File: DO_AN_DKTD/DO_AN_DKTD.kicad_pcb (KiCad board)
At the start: 2 copper layers, 90.2 x 65.7 mm, 60 parts, among them J1 Conn_01x03, J2 Conn_01x02, J3 Conn_01x07, J4 Conn_01x04, J5 Conn_01x02, Q1 NPN, Q2 NPN, Q3 NPN, Q4 NPN, SW2 RotaryEncoder_Switch, U1 AMS1117, U2 74HC595, U3 MOC3020M, U4 PC817, U5 DevKitSTM32

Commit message: code update
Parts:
- added R30: 4k7, IVS_FOOTPRINTS:R0603, B.Cu at (161.3, 125.4)
- added R31: 4k7, IVS_FOOTPRINTS:R0603, B.Cu at (161.3, 122.3)
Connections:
- U5 pad 11: /SER -> unconnected-(U5-PA6-Pad11)
- U5 pad 12: /OE -> unconnected-(U5-PA7-Pad12)
- U5 pad 26: unconnected-(U5-PB7-Pad26) -> /OE
- U5 pad 27: unconnected-(U5-PB6-Pad27) -> /SER
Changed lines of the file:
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@@
   (net 62 "unconnected-(U5-3v3-Pad18)")
   (net 63 "unconnected-(U5-3v3-Pad21)")
-  (net 64 "unconnected-(U5-PB6-Pad27)")
+  (net 64 "unconnected-(U5-PA6-Pad11)")
   (net 65 "unconnected-(U5-PB5-Pad28)")
   (net 66 "unconnected-(U5-PA12-Pad32)")
@@
   (net 81 "unconnected-(U5-PA4-Pad9)")
   (net 82 "unconnected-(U5-PA5-Pad10)")
-  (net 83 "unconnected-(U5-PB7-Pad26)")
+  (net 83 "unconnected-(U5-PA7-Pad12)")
   (net 84 "Net-(R15-Pad1)")
   (net 85 "/5vin")
@@
       (net 82 "unconnected-(U5-PA5-Pad10)") (pinfunction "PA5") (pintype "input+no_connect"))
     (pad "11" thru_hole circle (at -7.62 2.54 270) (size 1.524 1.524) (drill 0.762) (layers "*.Cu" "*.Mask")
-      (net 45 "/SER") (pinfunction "PA6") (pintype "input"))
+      (net 64 "unconnected-(U5-PA6-Pad11)") (pinfunction "PA6") (pintype "input+no_connect"))
     (pad "12" thru_hole circle (at -7.62 5.08 270) (size 1.524 1.524) (drill 0.762) (layers "*.Cu" "*.Mask")
-      (net 48 "/OE") (pinfunction "PA7") (pintype "input"))
+      (net 83 "unconnected-(U5-PA7-Pad12)") (pinfunction "PA7") (pintype "input+no_connect"))
     (pad "13" thru_hole circle (at -7.62 7.62 270) (size 1.524 1.524) (drill 0.762) (layers "*.Cu" "*.Mask")
       (net 53 "/AC_DET") (pinfunction "PB0") (pintype "input"))
@@
       (net 47 "/RCLK") (pinfunction "PB8") (pintype "input"))
     (pad "26" thru_hole circle (at 7.62 -10.16 270) (size 1.524 1.524) (drill 0.762) (layers "*.Cu" "*.Mask")
-      (net 83 "unconnected-(U5-PB7-Pad26)") (pinfunction "PB7") (pintype "input+no_connect"))
+      (net 48 "/OE") (pinfunction "PB7") (pintype "input"))
     (pad "27" thru_hole circle (at 7.62 -7.62 270) (size 1.524 1.524) (drill 0.762) (layers "*.Cu" "*.Mask")
-      (net 64 "unconnected-(U5-PB6-Pad27)") (pinfunction "PB6") (pintype "input+no_connect"))
+      (net 45 "/SER") (pinfunction "PB6") (pintype "input"))
     (pad "28" thru_hole circle (at 7.62 -5.08 270) (size 1.524 1.524) (drill 0.762) (layers "*.Cu" "*.Mask")
       (net 65 "unconnected-(U5-PB5-Pad28)") (pinfunction "PB5") (pintype "input+no_connect"))
@@
   )
   (footprint "IVS_FOOTPRINTS:R0603" (layer "B.Cu")
+    (at 161.255 125.4)
+    (descr "Resistor SMD 0603 (1608 Metric), square (rectangular) end terminal, IPC_7351 nominal, (Body size source: IPC-SM-782 page 72, https://www.pcb-3d.com/wordpress/wp-content/uploads/ipc-sm-782a_amendment_1_and_2.pdf), generated with kicad-footprint-generator")
+    (tags "resistor")
+    (property "Sheetfile" "DO_AN_DKTD.kicad_sch")
+    (property "Sheetname" "")
+    (property "ki_description" "Resistor")
+    (property "ki_keywords" "R res resistor")
+    (attr smd)
+    (fp_text reference "R30" (at -0.025 -1.5) (layer "B.SilkS")
+        (effects (font (size 0.6 0.6) (thickness 0.15)) (justify mirror))
+    )
+    (fp_text value "4k7" (at 0 -1.43) (layer "B.Fab") hide
+        (effects (font (size 1 1) (thickness 0.15)) (justify mirror))
+    )
+    (fp_text user "${REFERENCE}" (at 0 0) (layer "B.Fab") hide
+        (effects (font (size 0.4 0.4) (thickness 0.06)) (justify mirror))
+    )
+    (fp_rect (start -1.63 0.85) (end 1.63 -0.9)
+      (stroke (width 0.25) (type solid)) (fill none) (layer "B.SilkS"))
+    (fp_rect (start -1.78 1) (end 1.795 -1.05)
+      (stroke (width 0.05) (type solid)) (fill none) (layer "B.CrtYd"))
+    (fp_line (start -0.805 -0.4125) (end -0.805 0.4125)
+      (stroke (width 0.1) (type solid)) (layer "B.Fab"))
+    (fp_line (start -0.805 0.4125) (end 0.795 0.4125)
+      (stroke (width 0.1) (type solid)) (layer "B.Fab"))
+    (fp_line (start 0.795 -0.4125) (end -0.805 -0.4125)
+      (stroke (width 0.1) (type solid)) (layer "B.Fab"))
+    (fp_line (start 0.795 0.4125) (end 0.795 -0.4125)
+      (stroke (width 0.1) (type solid)) (layer "B.Fab"))
+    (pad "1" smd roundrect (at -0.83 0) (size 1 1) (layers "B.Cu" "B.Paste" "B.Mask") (roundrect_rratio 0.25)
+      (net 3 "+3V3") (pintype "passive"))
+    (pad "2" smd roundrect (at 0.82 0) (size 1 1) (layers "B.Cu" "B.Paste" "B.Mask") (roundrect_rratio 0.25)
+      (net 21 "/SCL") (pintype "passive"))
+    (model "${IOTVISION_3D}/RESISTOR/Resistor 0603.step"
+      (offset (xyz -0.75 1.15 0))
+      (scale (xyz 1 1 1))
+      (rotate (xyz -90 0 0))
+    )
+  )
+  (footprint "IVS_FOOTPRINTS:R0603" (layer "B.Cu")
     (at 144.7825 106.625 180)
     (descr "Resistor SMD 0603 (1608 Metric), square (rectangular) end terminal, IPC_7351 nominal, (Body size source: IPC-SM-782 page 72, https://www.pcb-3d.com/wordpress/wp-content/uploads/ipc-sm-782a_amendment_1_and_2.pdf), generated with kicad-footprint-generator")
@@
       (scale (xyz 1 1 1))
       (rotate (xyz -90 0 0))
+    )
+  )
+  (footprint "IVS_FOOTPRINTS:R0603" (layer "B.Cu")
+    (at 161.255 122.3)
+    (descr "Resistor SMD 0603 (1608 Metric), square (rectangular) end terminal, IPC_7351 nominal, (Body size source: IPC-SM-782 page 72, https://www.pcb-3d.com/wordpress/wp-content/uploads/ipc-sm-782a_amendment_1_and_2.pdf), generated with kicad-footprint-generator")
+    (tags "resistor")
+    (property "Sheetfile" "DO_AN_DKTD.kicad_sch")
+    (property "Sheetname" "")
+    (property "ki_description" "Resistor")
+    (property "ki_keywords" "R res resistor")
+    (attr smd)
+    (fp_text reference "R31" (at -0.025 -1.5) (layer "B.SilkS")
+        (effects (font (size 0.6 0.6) (thickness 0.15)) (justify mirror))
+    )
+    (fp_text value "4k7" (at 0 -1.43) (layer "B.Fab") hide
+        (effects (font (size 1 1) (thickness 0.15)) (justify mirror))
+    )
+    (fp_text user "${REFERENCE}" (at 0 0) (layer "B.Fab") hide
+        (effects (font (size 0.4 0.4) (thickness 0.06)) (justify mirror))
+    )
+    (fp_rect (start -1.63 0.85) (end 1.63 -0.9)
+      (stroke (width 0.25) (type solid)) (fill none) (layer "B.SilkS"))
+    (fp_rect (start -1.78 1) (end 1.795 -1.05)
+      (stroke (width 0.05) (type solid)) (fill none) (layer "B.CrtYd"))
+    (fp_line (start -0.805 -0.4125) (end -0.805 0.4125)
+      (stroke (width 0.1) (type solid)) (layer "B.Fab"))
+    (fp_line (start -0.805 0.4125) (end 0.795 0.4125)
+      (stroke (width 0.1) (type solid)) (layer "B.Fab"))
+    (fp_line (start 0.795 -0.4125) (end -0.805 -0.4125)
+      (stroke (width 0.1) (type solid)) (layer "B.Fab"))
+    (fp_line (start 0.795 0.4125) (end 0.795 -0.4125)
+      (stroke (width 0.1) (type solid)) (layer "B.Fab"))
+    (pad "1" smd roundrect (at -0.83 0) (size 1 1) (layers "B.Cu" "B.Paste" "B.Mask") (roundrect_rratio 0.25)
+      (net 3 "+3V3") (pintype "passive"))
+    (pad "2" smd roundrect (at 0.82 0) (size 1 1) (layers "B.Cu" "B.Paste" "B.Mask") (roundrect_rratio 0.25)
+      (net 22 "/SDA") (pintype "passive"))
+    (model "${IOTVISION_3D}/RESISTOR/Resistor 0603.step"
+      (offset (xyz -0.75 1.15 0))
+      (scale (xyz 1 1 1))
+      (rotate (xyz -90 0 0))

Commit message: completed layout PCB Ver 1.0
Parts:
- added BT1: CR1220, IVS_FOOTPRINTS:BatteryHolder_CR1220, F.Cu at (137.0, 80.0)
- added BZ1: Buzzer, Buzzer_Beeper:Buzzer_12x9.5RM7.6, F.Cu at (137.5, 96.6)
- added C10: 100nF, IVS_FOOTPRINTS:C_0603, F.Cu at (130.5, 126.5)
- added C11: 100nF, IVS_FOOTPRINTS:C_0603, F.Cu at (145.9, 113.0)
- added C12: 22pF, IVS_FOOTPRINTS:C_0603, F.Cu at (126.5, 115.0)
- added C13: 22pF, IVS_FOOTPRINTS:C_0603, F.Cu at (126.5, 112.0)
- added C14: 10uF, IVS_FOOTPRINTS:C_0603, F.Cu at (119.1, 89.0)
- added C15: 1uF, IVS_FOOTPRINTS:C_0603, F.Cu at (164.2, 129.3)
- added C16: 1uF, IVS_FOOTPRINTS:C_0603, F.Cu at (144.7, 125.7)
- added C17: 1uF, IVS_FOOTPRINTS:C_0603, F.Cu at (148.0, 125.7)
- added C18: 1uF, IVS_FOOTPRINTS:C_0603, F.Cu at (151.4, 125.7)
- added C19: 100nF, IVS_FOOTPRINTS:C_0603, F.Cu at (119.1, 90.7)
- added C20: 10uF, IVS_FOOTPRINTS:C_0603, F.Cu at (119.1, 92.5)
- added C21: 100nF, IVS_FOOTPRINTS:C_0603, F.Cu at (119.1, 94.0)
- added C22: 1uF, IVS_FOOTPRINTS:C_0603, F.Cu at (118.0, 138.5)
- added C23: 100nF, IVS_FOOTPRINTS:C_0603, F.Cu at (116.5, 138.5)
- added C24: 10uF, IVS_FOOTPRINTS:C_0805, F.Cu at (127.5, 65.8)
- added C25: 1uF, IVS_FOOTPRINTS:C_0603, F.Cu at (125.4, 65.8)
- added C26: 100nF, IVS_FOOTPRINTS:C_0603, F.Cu at (128.2, 69.2)
- added C27: 10uF, IVS_FOOTPRINTS:C_0805, F.Cu at (112.5, 53.7)
- added C29: 1uF, IVS_FOOTPRINTS:C_0603, F.Cu at (164.2, 133.0)
- added C30: 1uF, IVS_FOOTPRINTS:C_0603, F.Cu at (164.2, 139.2)
- added C31: 1uF, IVS_FOOTPRINTS:C_0603, F.Cu at (168.4, 122.8)
- added C32: 100nF, IVS_FOOTPRINTS:C_0603, F.Cu at (168.4, 124.2)
- added C33: 100nF, IVS_FOOTPRINTS:C_0603, F.Cu at (111.0, 115.8)
- added C34: 100nF, IVS_FOOTPRINTS:C_0603, F.Cu at (120.0, 118.8)
- added C35: 100nF, IVS_FOOTPRINTS:C_0603, F.Cu at (112.2, 107.8)
- added C36: 100nF, IVS_FOOTPRINTS:C_0603, F.Cu at (123.3, 110.6)
- added D+: TestPoint, TestPoint:TestPoint_THTPad_D2.0mm_Drill1.0mm, F.Cu at (100.4, 103.8)
- added D-: TestPoint, TestPoint:TestPoint_THTPad_D2.0mm_Drill1.0mm, F.Cu at (102.9, 103.8)
- added D4: BAT54C, IVS_FOOTPRINTS:SOT23-3, F.Cu at (120.8, 74.2)
- added D5: SMF05C, IVS_FOOTPRINTS:TSSOP-6, F.Cu at (122.1, 135.1)
- added D6: SS54, IVS_FOOTPRINTS:D_SMA, F.Cu at (120.0, 61.3)
- added D7: D_Schottky, IVS_FOOTPRINTS:D_SOD323, F.Cu at (125.2, 69.3)
- added D8: SS54, IVS_FOOTPRINTS:D_SMA, F.Cu at (132.6, 64.2)
- added F3: Fuse, IVS_FOOTPRINTS:Fuse_1812_4532Metric, F.Cu at (141.8, 59.2)
- added G***: LOGO, IVS_FOOTPRINTS:LoGo_ST_2.5x1.5mm, F.Cu at (158.1, 129.8)
- added G***: LOGO, IVS_FOOTPRINTS:LoGo_IDF_2.5x2.5mm, F.Cu at (158.1, 138.3)
- added G***: LOGO, IVS_FOOTPRINTS:LoGo_1412_10x8mm, F.Cu at (110.6, 121.7)
- added G***: LOGO, IVS_FOOTPRINTS:LoGo_ST_2.5x1.5mm, F.Cu at (117.0, 112.8)
- added G***: LOGO, IVS_FOOTPRINTS:LoGo_IDF_2.5x2.5mm, F.Cu at (179.3, 134.3)
- added G***: LOGO, IVS_FOOTPRINTS:LoGo_1412_10x8mm, B.Cu at (164.6, 68.3)
- added IC1: RTC_DS3231M, IVS_FOOTPRINTS:SOIC-16W_7.5x10.3mm_P1.27mm, F.Cu at (121.5, 82.0)
- added J10: Jack-DC, IVS_FOOTPRINTS:BarrelJack_Wuerth_6941xx301002, F.Cu at (134.2, 55.2)
- added J6: , Connector_PinHeader_2.54mm:PinHeader_1x06_P2.54mm_Vertical, F.Cu at (180.8, 120.0)
- added J7: Conn_01x05_Male, Connector_PinHeader_2.54mm:PinHeader_1x05_P2.54mm_Vertical, F.Cu at (109.8, 88.0)
- added J8: Micro_SD_Card_Det1, IVS_FOOTPRINTS:MicroSD_Socket_9P, F.Cu at (132.4, 139.8)
- added J9: USB_C_Receptacle, IVS_FOOTPRINTS:USB_C_Receptacle_XKB_U262-16XN-4BVC11, F.Cu at (101.0, 110.8)
- added L1: 68uH 2A, IVS_FOOTPRINTS:L_10.4x10.4_H4.8, F.Cu at (122.0, 53.5)
- added LE2: 5631AS, IVS_FOOTPRINTS:7Segment_4led_Cathode_30x14mm, F.Cu at (175.7, 108.5)
- added LE3: Led, IVS_FOOTPRINTS:LED_0603, F.Cu at (136.6, 115.8)
- added LE4: Led, IVS_FOOTPRINTS:LED_0603, F.Cu at (132.6, 115.8)
- added LE5: Led, IVS_FOOTPRINTS:LED_0603, F.Cu at (134.6, 115.8)
- added LE6: Led, IVS_FOOTPRINTS:LED_0603, F.Cu at (106.5, 93.5)
- added LE7: Led, IVS_FOOTPRINTS:LED_0603, F.Cu at (106.2, 48.8)
- added LE8: Led, IVS_FOOTPRINTS:LED_0603, F.Cu at (106.2, 50.2)
- added LE9: Led, IVS_FOOTPRINTS:LED_0603, F.Cu at (106.5, 100.0)
- added MI: TestPoint, TestPoint:TestPoint_THTPad_D2.0mm_Drill1.0mm, F.Cu at (120.3, 142.9)
- added MO: TestPoint, TestPoint:TestPoint_THTPad_D2.0mm_Drill1.0mm, F.Cu at (120.3, 137.8)
- added Q10: P_Mosfet, IVS_FOOTPRINTS:SOT23-3, F.Cu at (132.8, 67.5)
- added Q5: NPN, IVS_FOOTPRINTS:SOT23-3, F.Cu at (157.5, 110.1)
- added Q6: NPN, IVS_FOOTPRINTS:SOT23-3, F.Cu at (157.5, 106.7)
- added Q7: NPN, IVS_FOOTPRINTS:SOT23-3, F.Cu at (157.5, 103.3)
- added Q8: NPN, IVS_FOOTPRINTS:SOT23-3, F.Cu at (157.5, 113.7)
- added Q9: N_Mosfet, IVS_FOOTPRINTS:SOT23-3, F.Cu at (125.2, 97.5)
- added R32: 12k, IVS_FOOTPRINTS:R_0603, F.Cu at (126.7, 69.2)
- added R36: 2k, IVS_FOOTPRINTS:R_0603, F.Cu at (154.7, 110.1)
- added R37: 2k, IVS_FOOTPRINTS:R_0603, F.Cu at (154.7, 106.7)
- added R38: 2k, IVS_FOOTPRINTS:R_0603, F.Cu at (154.7, 103.3)
- added R39: 2k, IVS_FOOTPRINTS:R_0603, F.Cu at (154.7, 113.7)
- added R40: 1M, IVS_FOOTPRINTS:R_0603, F.Cu at (125.0, 113.8)
- added R41: 1k, IVS_FOOTPRINTS:R_0603, F.Cu at (123.5, 74.2)
- added R42: 100, IVS_FOOTPRINTS:R_0603, F.Cu at (164.0, 122.8)
- added R43: 10k, IVS_FOOTPRINTS:R_0603, F.Cu at (164.2, 136.0)
- added R44: 1k, IVS_FOOTPRINTS:R_0603, F.Cu at (136.6, 112.3)
- added R45: 10k, IVS_FOOTPRINTS:R_0603, F.Cu at (164.2, 142.2)
- added R46: 10k, IVS_FOOTPRINTS:R_0603, F.Cu at (164.2, 126.3)
- added R47: 1k, IVS_FOOTPRINTS:R_0603, F.Cu at (132.6, 112.2)
- added R48: 1k, IVS_FOOTPRINTS:R_0603, F.Cu at (134.6, 112.2)
- added R50: 1k, IVS_FOOTPRINTS:R_0603, F.Cu at (109.2, 48.8)
- added R51: 1k, IVS_FOOTPRINTS:R_0603, F.Cu at (109.2, 50.2)
- added R55: 4k7, IVS_FOOTPRINTS:R_0603, F.Cu at (111.0, 110.8)
- added R58: 100R, IVS_FOOTPRINTS:R_0603, F.Cu at (112.2, 106.3)
- added R59: 100R, IVS_FOOTPRINTS:R_0603, F.Cu at (122.6, 108.1)
- added R60: 1M, IVS_FOOTPRINTS:R_0603, F.Cu at (125.2, 100.4)
- added R61: 10K, IVS_FOOTPRINTS:R_0603, F.Cu at (115.8, 104.5)
- added R62: 10K, IVS_FOOTPRINTS:R_0603, F.Cu at (120.0, 120.2)
- added REF**: MountingHole_3.2mm_M3_Pad_Via, MountingHole:MountingHole_3.2mm_M3_Pad_Via, F.Cu at (186.5, 121.2)
- added REF**: MountingHole_3.2mm_M3_Pad_Via, MountingHole:MountingHole_3.2mm_M3_Pad_Via, F.Cu at (186.5, 72.8)
- added REF**: MountingHole_3.2mm_M3_Pad_Via, MountingHole:MountingHole_3.2mm_M3_Pad_Via, F.Cu at (101.5, 121.2)
- added REF**: MountingHole_3.2mm_M3_Pad_Via, MountingHole:MountingHole_3.2mm_M3_Pad_Via, F.Cu at (101.5, 72.8)
- added SCK: TestPoint, TestPoint:TestPoint_THTPad_D2.0mm_Drill1.0mm, F.Cu at (120.3, 140.3)
- added SW1: RotaryEncoder_Switch, IVS_FOOTPRINTS:RotaryEncoder_Alps_EC11E-Switch_Vertical_H20mm, F.Cu at (149.8, 135.7)
- added SW3: SW_Push, IVS_FOOTPRINTS:SW_SPST_PTS810, F.Cu at (161.5, 134.5)
- added SW4: SW_Push, IVS_FOOTPRINTS:SW_SPST_PTS810, F.Cu at (161.5, 127.8)
- added U10: ESP-07, IVS_FOOTPRINTS:ESP8266-07__ESP32-C3-12F, F.Cu at (184.2, 126.1)
- added U6: 74HC595, IVS_FOOTPRINTS:SOIC-16W_3.92x10.2mm, F.Cu at (147.9, 107.0)
- added U7: STM32F103C8Tx, IVS_FOOTPRINTS:LQFP-48_7x7mm_P0.5mm, F.Cu at (117.0, 112.8)
- added U8: 24C32N, IVS_FOOTPRINTS:SOIC-8_3.9x4.9mm_P1.27mm, F.Cu at (120.2, 98.5)
- added U9: Ai-Thinker-Ra-02, IVS_FOOTPRINTS:MODULE_RA-02_LORA, F.Cu at (106.2, 134.8)
- added Y1: Crystal_GND24_Small, IVS_FOOTPRINTS:Crystal_3225_4P_3.2x2.6mm, F.Cu at (129.0, 113.2)
- C1: value 100nF -> 1uF; moved to F.Cu
- C2: value 1uF -> 100nF; moved to F.Cu
- C3, C4, C6, C9, D3, F2, Q1, Q2, Q3, Q4, U1: moved to F.Cu
- C5: value 50nF -> 10nF; moved to F.Cu
- C7: value 10nF -> 10uF; moved to F.Cu
- C8: value 10uF -> 50nF; moved to F.Cu
- D1: value TRIAC -> MB10F; footprint IVS_FOOTPRINTS:TO-220-3_Vertical -> IVS_FOOTPRINTS:Bridge_MB10F-13
- D2: value MB10F -> TRIAC; footprint IVS_FOOTPRINTS:Bridge_MB10F-13 -> IVS_FOOTPRINTS:TO-220-3_Vertical; moved to F.Cu
- F1: footprint IVS_FOOTPRINTS:Fuse_BLX-A-P22.4mm -> IVS_FOOTPRINTS:Fuseholder_Littelfuse_Nano2_154x
- J1: value Conn_01x03 -> Conn_01x07; footprint IVS_FOOTPRINTS:Conn_XH-P2.54mm-3P -> IVS_FOOTPRINTS:Conn_XH-P2.54mm-7P
- J3: value Conn_01x07 -> Conn_01x04; footprint IVS_FOOTPRINTS:Conn_XH-P2.54mm-7P -> IVS_FOOTPRINTS:Conn_XH-P2.54mm-4P
- J4: value Conn_01x04 -> Conn_01x03; footprint IVS_FOOTPRINTS:Conn_XH-P2.54mm-4P -> IVS_FOOTPRINTS:Conn_XH-P2.54mm-3P
- R1, R10, R11, R2, R20, R3: footprint IVS_FOOTPRINTS:R0603 -> IVS_FOOTPRINTS:R_0603; moved to F.Cu
- R12, R13, R14: value 2k -> 1k; footprint IVS_FOOTPRINTS:R0603 -> IVS_FOOTPRINTS:R_0603; moved to F.Cu
- R15, R16, R17, R30, R31: value 4k7 -> 1k; footprint IVS_FOOTPRINTS:R0603 -> IVS_FOOTPRINTS:R_0603; moved to F.Cu
- R18: value 4k7 -> 2k; footprint IVS_FOOTPRINTS:R0603 -> IVS_FOOTPRINTS:R_0603; moved to F.Cu
- R19: value 360 -> 39; footprint IVS_FOOTPRINTS:R0805 -> IVS_FOOTPRINTS:R_0603; moved to F.Cu
- R21: value 39 -> 22k; footprint IVS_FOOTPRINTS:R0603 -> IVS_FOOTPRINTS:R_0603; moved to F.Cu
- R22: value 360 -> 1k; footprint IVS_FOOTPRINTS:R0603 -> IVS_FOOTPRINTS:R_0603; moved to F.Cu
- R23: value 180k -> 360; footprint IVS_FOOTPRINTS:R0603 -> IVS_FOOTPRINTS:R_0805; moved to F.Cu
- R24: value 180k -> 1k; footprint IVS_FOOTPRINTS:R0603 -> IVS_FOOTPRINTS:R_0603; moved to F.Cu
- R25: value 1k -> 360; footprint IVS_FOOTPRINTS:R0603 -> IVS_FOOTPRINTS:R_0603; moved to F.Cu
- R26: value 22k -> 4k7; footprint IVS_FOOTPRINTS:R0603 -> IVS_FOOTPRINTS:R_0603; moved to F.Cu
- R27, R4, R5, R7, R8: value 1k -> 4k7; footprint IVS_FOOTPRINTS:R0603 -> IVS_FOOTPRINTS:R_0603; moved to F.Cu
- R28, R29: value 0R -> 2k; footprint IVS_FOOTPRINTS:R0805 -> IVS_FOOTPRINTS:R_0603; moved to F.Cu
- R6, R9: value 1k -> 180k; footprint IVS_FOOTPRINTS:R0603 -> IVS_FOOTPRINTS:R_0603; moved to F.Cu
- SW2: value RotaryEncoder_Switch -> SW_Push; footprint IVS_FOOTPRINTS:RotaryEncoder_Alps_EC11E-Switch_Vertical_H20mm -> IVS_FOOTPRINTS:SW_SPST_PTS810
- U2: footprint IVS_FOOTPRINTS:SOIC-16W_5.3x10.2mm_P1.27mm -> IVS_FOOTPRINTS:SOIC-16W_3.92x10.2mm; moved to F.Cu
- U3: value MOC3020M -> PC817; footprint IVS_FOOTPRINTS:DIL06-E -> IVS_FOOTPRINTS:OPTO_SOT254P975X400-4N
- U4: value PC817 -> MOC3020M; footprint IVS_FOOTPRINTS:OPTO_SOT254P975X400-4N -> IVS_FOOTPRINTS:DIL06-E; moved to F.Cu
- U5: value DevKitSTM32 -> XL1509; footprint IVS_FOOTPRINTS:DevKitSTM32 -> IVS_FOOTPRINTS:SOIC-8_3.9x4.9mm_P1.27mm
- moved J1 94.5 mm to (100.5, 57.9), turned to 0 degrees
- moved F2 92.3 mm to (108.0, 53.5), turned to 0 degrees
- moved U5 88.2 mm to (121.4, 67.0)
- moved C2 84.8 mm to (111.0, 58.5), turned to 0 degrees
- moved J3 84.7 mm to (101.2, 84.2), turned to 0 degrees
- moved C1 83.6 mm to (111.0, 56.8), turned to 180 degrees
- moved U1 76.9 mm to (109.0, 64.0), turned to 180 degrees
- moved D2 76.4 mm to (169.3, 50.2), turned to -90 degrees
- moved C8 69.5 mm to (163.2, 50.2), turned to 0 degrees
- moved C4 68.5 mm to (109.7, 70.9), turned to 0 degrees
- moved J5 67.8 mm to (184.8, 63.0)
- moved J2 67.7 mm to (184.8, 52.8)
- moved C3 66.9 mm to (109.7, 69.2), turned to 180 degrees
- moved C6 65.1 mm to (178.0, 51.8), turned to 90 degrees
- moved REF** 64.8 mm to (160.9, 56.4)
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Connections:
- C1 pad 1: +5V -> GND
- C1 pad 2: GND -> +5V
- C2 pad 1: GND -> +5V
- C2 pad 2: +5V -> GND
- C5 pad 2: Net-(D1-A1) -> Net-(C5-Pad2)
- C6 pad 2: Net-(D1-A1) -> /Peripheral/Load
- C7 pad 1: Net-(C7-Pad1) -> Net-(D1-+)
- C7 pad 2: Net-(C7-Pad2) -> Net-(Q4-E)
- C8 pad 1: Net-(D2-+) -> Net-(C8-Pad1)
- C8 pad 2: Net-(Q4-E) -> /Peripheral/Load
- C9 pad 2: Net-(U2-VCC) -> +5V
- D1 pad 1: Net-(D1-A1) -> Net-(D1-+)
- D1 pad 2: Net-(D1-A2) -> Net-(C5-Pad2)
- D1 pad 3: Net-(D1-G) -> Net-(D1--)
- D2 pad 1: Net-(D2-+) -> /Peripheral/Load
- D2 pad 2: Net-(C7-Pad2) -> /Peripheral/L_after
- D2 pad 3: Net-(D2--) -> Net-(D2-G)
- D3 pad 2: Net-(D2--) -> Net-(D1--)
- F1 pad 1: Net-(D1-A2) -> /Peripheral/L_after
- F1 pad 2: /L -> /Peripheral/L
- F2 pad 1: /5vin -> /POWER/5vin
- J1 pad 1: /TX -> unconnected-(J1-Pin_1-Pad1)
- J1 pad 2: /RX -> /POWER/5vin
- J1 pad 3: GND -> /POWER/5vin
- J2 pad 1: /N -> /Peripheral/N
- J2 pad 2: /L -> /Peripheral/Load
- J3 pad 1: unconnected-(J3-Pin_1-Pad1) -> +3V3
- J3 pad 2: /5vin -> /Peripheral/24C32.SCL
- J3 pad 3: /5vin -> /Peripheral/24C32.SDA
- J4 pad 1: +3V3 -> GND
- J4 pad 2: /SCL -> /Peripheral/LOG_RX
- J4 pad 3: /SDA -> /Peripheral/LOG_TX
- J5 pad 1: Net-(D1-A1) -> /Peripheral/L
- J5 pad 2: /N -> /Peripheral/N
- Q4 pad 1: Net-(D2--) -> Net-(D1--)
- R1 pad 2: /EnC_B -> /Peripheral/Encoder.EnC_BT
- R10 pad 1: Net-(U2-QA) -> Net-(U2-QH)
- R10 pad 2: Net-(LE1-g) -> Net-(LE1-a)
- R11 pad 1: Net-(U2-QG) -> Net-(U2-QF)
- R11 pad 2: Net-(LE1-DPX) -> Net-(LE1-b)
- R12 pad 1: /LE1 -> Net-(U2-QD)
- R12 pad 2: Net-(Q3-B) -> Net-(LE1-c)
- R13 pad 1: /LE2 -> Net-(U2-QB)
- R13 pad 2: Net-(Q2-B) -> Net-(LE1-d)
- R14 pad 1: /LE3 -> Net-(U2-QA)
- R14 pad 2: Net-(Q1-B) -> Net-(LE1-e)
- R15 pad 1: Net-(R15-Pad1) -> Net-(U2-QG)
- R15 pad 2: /SER -> Net-(LE1-f)
- R16 pad 1: +5V -> Net-(U2-QE)
- R16 pad 2: /SRCLK -> Net-(LE1-g)
- R17 pad 1: +5V -> Net-(U2-QC)
- R17 pad 2: /RCLK -> Net-(LE1-DPX)
- R18 pad 1: Net-(R15-Pad1) -> /Peripheral/LE3
- R18 pad 2: /OE -> Net-(Q3-B)
- R19 pad 1: Net-(R19-Pad1) -> /Peripheral/L_after
- R19 pad 2: Net-(C5-Pad1) -> Net-(C6-Pad1)
- R2 pad 2: /EnC_A -> /Peripheral/Encoder.EnC_B
- R20 pad 1: Net-(C5-Pad1) -> Net-(C8-Pad1)
- R20 pad 2: Net-(D1-A2) -> /Peripheral/L_after
- R21 pad 1: Net-(D1-A2) -> Net-(D1-+)
- R21 pad 2: Net-(C6-Pad1) -> Net-(D1--)
- R22 pad 1: /TRIAC -> Net-(R22-Pad1)
- R22 pad 2: Net-(R22-Pad2) -> Net-(D1-+)
- R23 pad 1: Net-(C7-Pad1) -> Net-(R23-Pad1)
- R23 pad 2: /L -> Net-(C8-Pad1)
- R24 pad 1: Net-(C7-Pad2) -> +3V3
- R24 pad 2: /N -> /Peripheral/AC_DET
- R25 pad 1: Net-(R25-Pad1) -> /Peripheral/TRIAC
- R25 pad 2: Net-(D2-+) -> Net-(R25-Pad2)
- R26 pad 1: Net-(D2-+) -> +3V3
- R26 pad 2: Net-(D2--) -> /Peripheral/24C32.SCL
- R27 pad 2: /AC_DET -> /Peripheral/24C32.SDA
- R28 pad 1: Net-(U2-VCC) -> /Peripheral/LE2
- R28 pad 2: Net-(R15-Pad1) -> Net-(Q2-B)
- R29 pad 1: Net-(R15-Pad1) -> /Peripheral/LE1
- R29 pad 2: +5V -> Net-(Q1-B)
- R3 pad 2: /EnC_BT -> /Peripheral/Encoder.EnC_A
- R30 pad 2: /SCL -> Net-(LE6-Pad1)
- R31 pad 2: /SDA -> Net-(LE9-Pad1)
- R4 pad 1: Net-(U2-QB) -> +5V
- R4 pad 2: Net-(LE1-a) -> /Peripheral/74HC595.RCLK
- R5 pad 1: Net-(U2-QD) -> +5V
- R5 pad 2: Net-(LE1-b) -> /Peripheral/74HC595.SRCLK
- R6 pad 1: Net-(U2-QH) -> Net-(C5-Pad1)
- R6 pad 2: Net-(LE1-c) -> /Peripheral/L_after
- R7 pad 1: Net-(U2-QF) -> +5V
- R7 pad 2: Net-(LE1-d) -> /Peripheral/74HC595.OE
- R8 pad 1: Net-(U2-QE) -> +5V
- R8 pad 2: Net-(LE1-e) -> /Peripheral/74HC595.SER
- R9 pad 1: Net-(U2-QC) -> Net-(C5-Pad2)
- R9 pad 2: Net-(LE1-f) -> /Peripheral/N
- U2 pad 10: Net-(U2-VCC) -> +5V
- U2 pad 11: /SRCLK -> /Peripheral/74HC595.SRCLK
- U2 pad 12: /RCLK -> /Peripheral/74HC595.RCLK
- U2 pad 13: /OE -> /Peripheral/74HC595.OE
- U2 pad 14: /SER -> Net-(U2-SER)
- U2 pad 16: Net-(U2-VCC) -> +5V
- U3 pad 1: Net-(R22-Pad2) -> Net-(R22-Pad1)
- U3 pad 2: GND -> Net-(Q4-C)
- U3 pad 3: unconnected-(U3-NC-Pad3) -> GND
- U3 pad 4: Net-(D1-G) -> /Peripheral/AC_DET
- U4 pad 1: Net-(R25-Pad1) -> Net-(R25-Pad2)
- U4 pad 2: Net-(Q4-C) -> GND
- U4 pad 3: GND -> unconnected-(U4-NC-Pad3)
- U4 pad 4: /AC_DET -> Net-(D2-G)
- U5 pad 1: unconnected-(U5-VBAT-Pad1) -> VDC
- U5 pad 2: unconnected-(U5-PC13-Pad2) -> /POWER/VOUT
- U5 pad 3: unconnected-(U5-PC14-Pad3) -> +5V
- U5 pad 4: unconnected-(U5-PC15-Pad4) -> GND
- U5 pad 5: /LE3 -> GND
- U5 pad 6: /LE2 -> GND
- U5 pad 7: /LE1 -> GND
- U5 pad 8: unconnected-(U5-PA3-Pad8) -> GND
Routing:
- net +3V3: track 112.5 -> 368.7 mm, vias 0 -> 22
- net GND: track 220.8 -> 2.42 mm, vias 0 -> 57
- net /Peripheral/TRIAC: track 0.00 -> 75.7 mm
- net /Peripheral/24C32.SCL: track 0.00 -> 72.8 mm, vias 0 -> 3
- net /Peripheral/24C32.SDA: track 0.00 -> 71.8 mm, vias 0 -> 3
- net /Peripheral/LORA.MISO: track 0.00 -> 68.3 mm, vias 0 -> 2
- net /ESP/TX_ESP32: track 0.00 -> 67.0 mm
- net /Peripheral/LORA.MOSI: track 0.00 -> 66.9 mm, vias 0 -> 2
- net /Peripheral/LORA.SCK: track 0.00 -> 66.9 mm, vias 0 -> 2
- net /STM32/RST: track 0.00 -> 64.5 mm, vias 0 -> 2
- net /Peripheral/Encoder.EnC_BT: track 0.00 -> 64.0 mm, vias 0 -> 2
- net /Peripheral/AC_DET: track 0.00 -> 61.4 mm
- net /Peripheral/SD.CS: track 0.00 -> 59.6 mm, vias 0 -> 2
- net /Peripheral/Encoder.EnC_A: track 0.00 -> 56.4 mm, vias 0 -> 1
- net /OE: track 54.7 -> 0.00 mm
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- added copper zone on F.Cu, net +3V3
- added copper zone on F.Cu, net +5V
- added copper zone on F.Cu, net /POWER/5vin
- added copper zone on F.Cu, net /POWER/A
- added copper zone on F.Cu, net /POWER/B
- added copper zone on F.Cu, net /POWER/VOUT
- added copper zone on F.Cu, net GND
- added copper zone on F.Cu, net VDC
- removed copper zone on B.Cu, net +3V3
- removed copper zone on B.Cu, net +5V
- removed copper zone on B.Cu, net /5vin
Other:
- board size 90.2 x 65.7 mm -> 96 x 97.2 mm
- board text added: "12V IN"
- board text added: "3V B RX TX R G"
- board text added: "3V SCL SDA G"
- board text added: "3V3"
- board text added: "5V"
- board text added: "5V 3V G IO CLK"
- board text added: "BOOT"
- board text added: "BORAD V0.1 Designed By Nguyen Trung Thao 20151564"
- board text added: "G RX TX"
- board text added: "RST"
- board text added: "USB"
- board text added: "~220V"
- board text removed: "POWER"
- board text removed: "SETUP"
- board text removed: "Temperature PID Nguyen Trung Thao 20151564"
- board text removed: "~220AC"

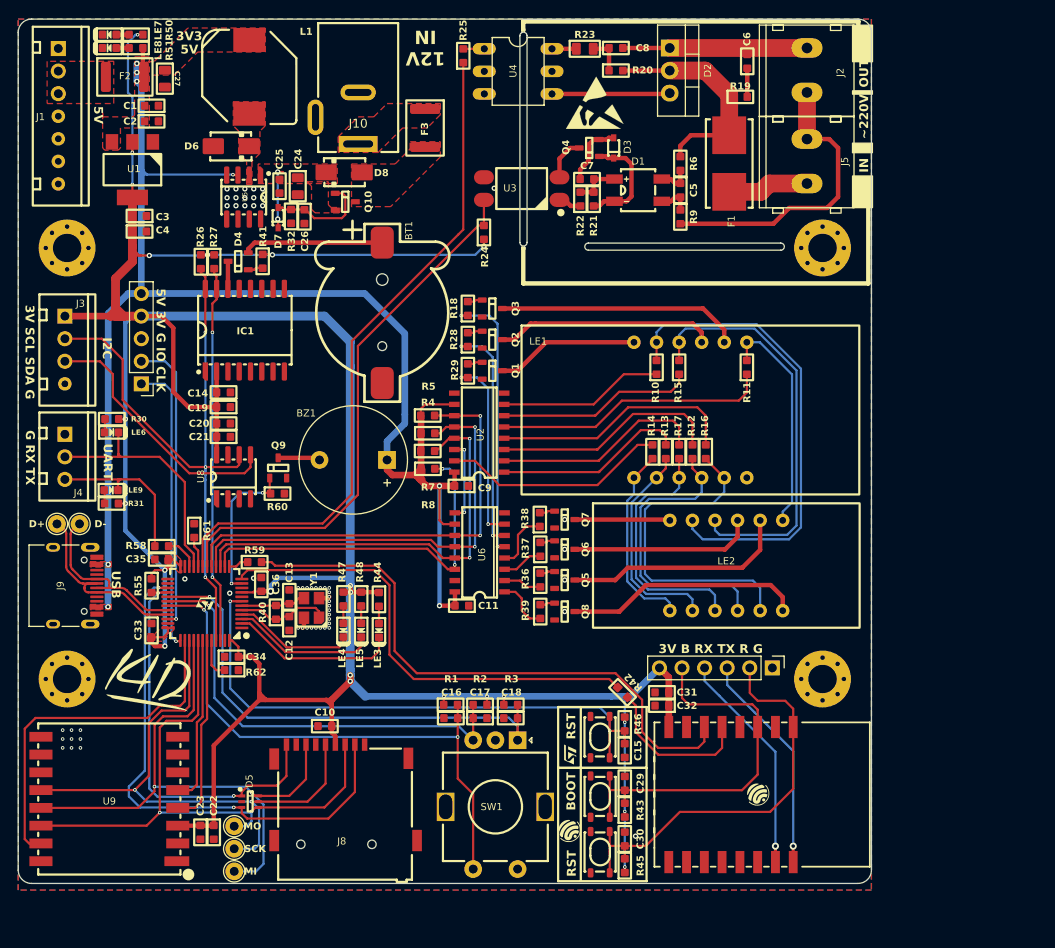
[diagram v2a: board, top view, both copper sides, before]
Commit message: add testoint SPI USB LEDTEST and Buck power
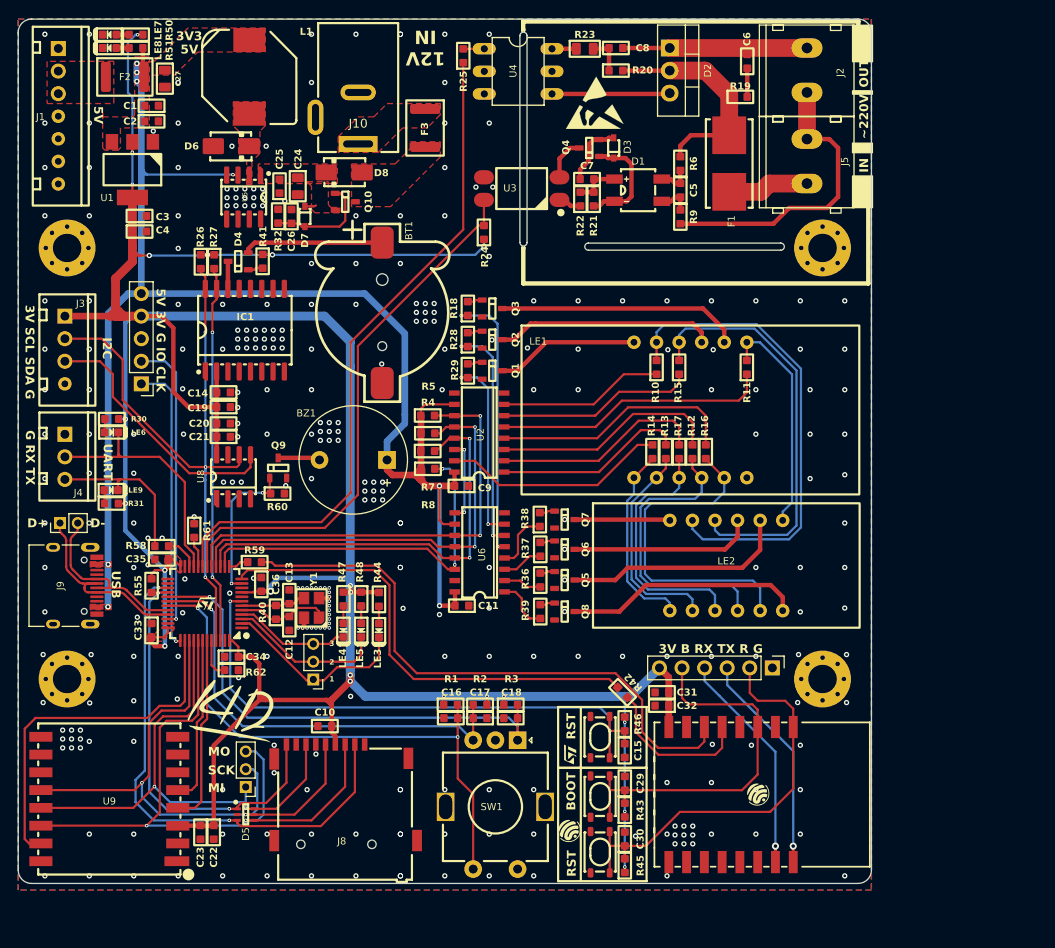
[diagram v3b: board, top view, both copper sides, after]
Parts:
- removed D+, D-, MI, MO, SCK: TestPoint, TestPoint:TestPoint_THTPad_D2.0mm_Drill1.0mm
- added J11: Conn_01x03_Pin, Connector_PinHeader_2.00mm:PinHeader_1x03_P2.00mm_Vertical, F.Cu at (129.2, 121.3)
- added J12: Conn_01x03_Pin, Connector_PinHeader_2.00mm:PinHeader_1x03_P2.00mm_Vertical, F.Cu at (121.6, 133.4)
- added J13: Conn_01x02_Pin, Connector_PinHeader_2.00mm:PinHeader_1x02_P2.00mm_Vertical, F.Cu at (100.7, 103.7)
- moved G*** 9.94 mm to (119.9, 125.2)
- moved D7 3.00 mm to (128.2, 69.2), turned to -90 degrees
- moved D5 1.54 mm to (121.6, 136.5)
- moved R32 1.45 mm to (125.2, 69.2), turned to 90 degrees
- moved C26 1.45 mm to (126.8, 69.2), turned to 90 degrees
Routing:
- net /Peripheral/LORA.MOSI: track 66.9 -> 76.7 mm
- net /Peripheral/LORA.MISO: track 68.3 -> 60.0 mm
- net VDC: track 6.91 -> 1.28 mm, vias 2 -> 0
- net /STM32/Led_test1: track 18.9 -> 21.5 mm
- net /Peripheral/SD.DET: track 44.9 -> 46.5 mm
- net /STM32/Led_test2: track 16.3 -> 17.7 mm
- net /STM32/Led_test3: track 13.8 -> 13.1 mm
- net /Peripheral/LORA.SCK: track 66.9 -> 67.4 mm
- net GND: vias 57 -> 309
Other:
- board text added: "1"
- board text added: "2"
- board text added: "3"
- board text added: "D+"
- board text added: "D-"
- board text added: "MI"
- board text added: "MO"
- board text added: "SCK"

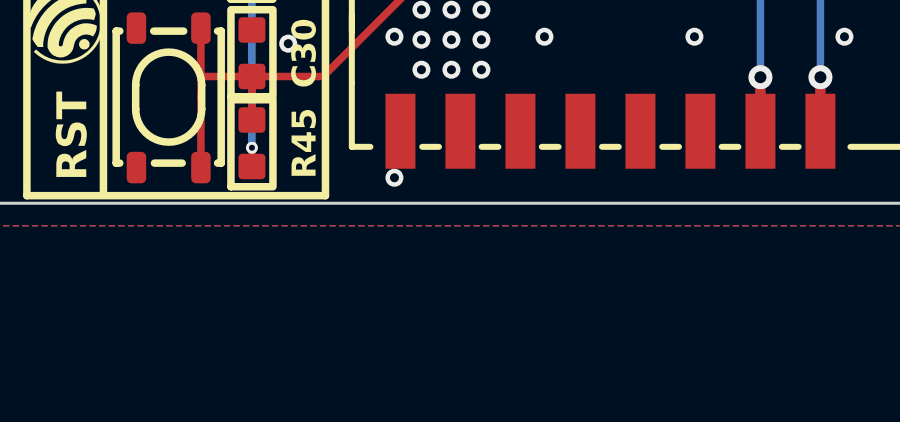
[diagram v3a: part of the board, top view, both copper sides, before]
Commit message: config pin STM32 CubeIDE, and add resistor ESP8266
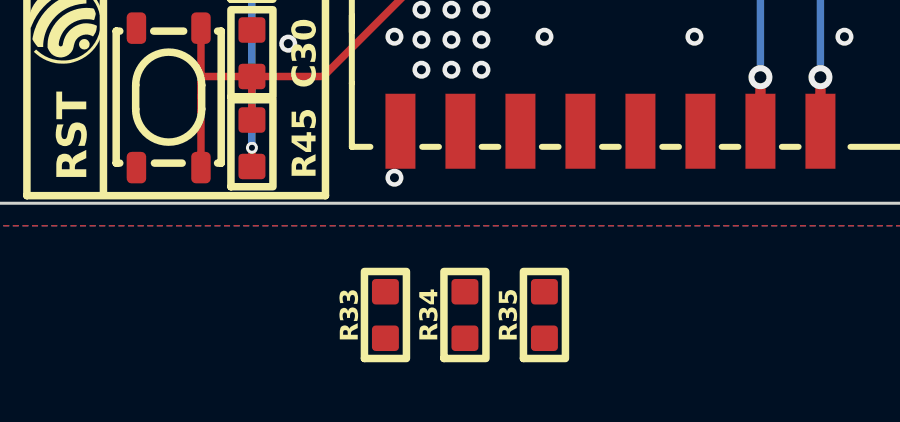
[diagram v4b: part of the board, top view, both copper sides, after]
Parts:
- added R33: 10k, IVS_FOOTPRINTS:R_0603, F.Cu at (168.7, 148.0)
- added R34: 10k, IVS_FOOTPRINTS:R_0603, F.Cu at (171.3, 148.0)
- added R35: 10k, IVS_FOOTPRINTS:R_0603, F.Cu at (174.0, 148.0)
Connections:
- U10 pad 16: unconnected-(U10-GPIO15-Pad16) -> Net-(U10-GPIO15)
- U10 pad 17: unconnected-(U10-GPIO2-Pad17) -> Net-(U10-GPIO2)
- U10 pad 18: unconnected-(U10-GPIO0-Pad18) -> /ESP/BOOT
- U10 pad 3: /ESP/BOOT -> Net-(U10-EN)
